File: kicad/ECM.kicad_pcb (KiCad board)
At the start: 2 copper layers, 84.1 x 61.7 mm, 82 parts, among them J1 Bus_PCI_Express_x1, J6 USB_C_Receptacle_USB2.0_16P, Q1 AO3400A, Q2 AO3400A, U1 MCP25625T-E/ML, U10 MAX31855KASA+T, U2 RP2040, U3 ADS8688IDBTR, U4 W25Q128JVP, U5 TPS22976DPUR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

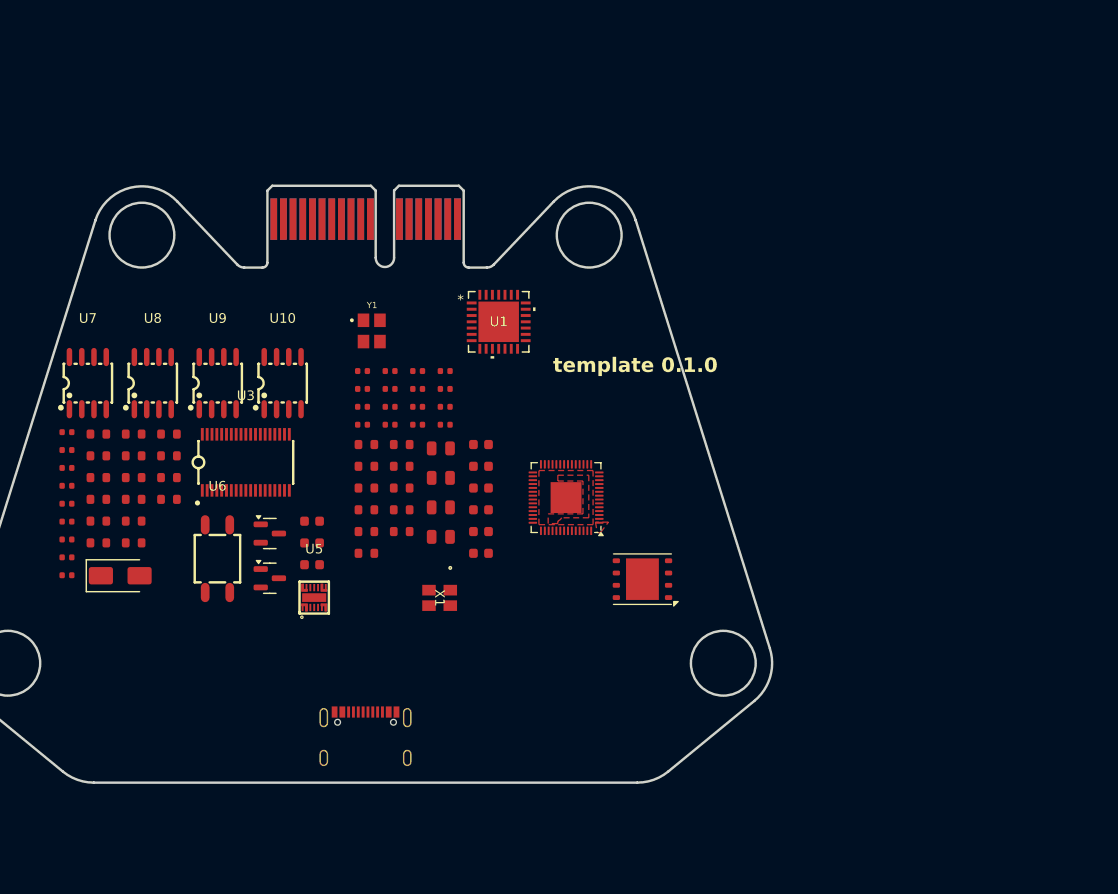
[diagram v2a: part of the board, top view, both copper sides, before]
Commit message: Preliminary PCB Layout on most ICs, carved out analog, power and digital regions.
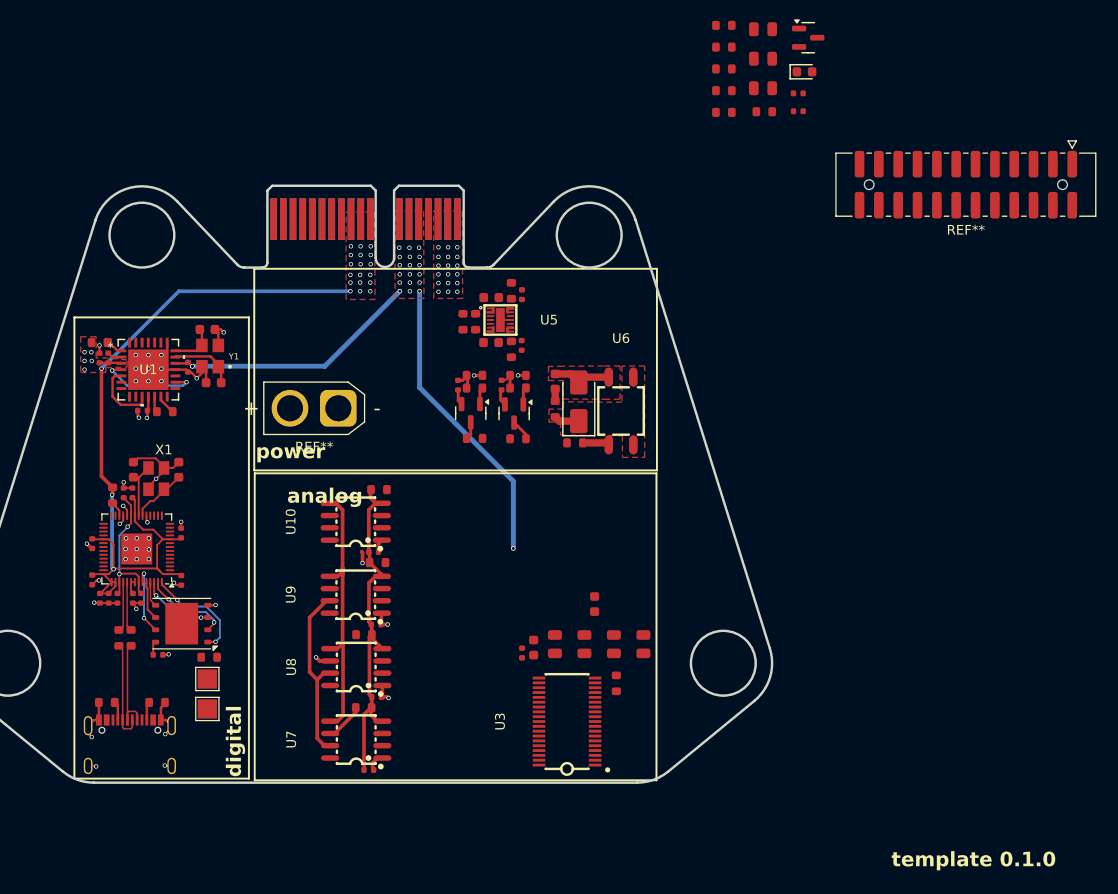
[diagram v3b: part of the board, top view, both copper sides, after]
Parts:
- removed the R7 at (150.2, 87.5)
- removed the R8 at (150.2, 89.7)
- added C36: 2.2uF, PCM_JLCPCB:C_0805, F.Cu at (187.5, 44.5)
- added C37: 100nF, PCM_JLCPCB:C_0402, F.Cu at (191.2, 51.1)
- added C38: 10uF, PCM_JLCPCB:C_0805, F.Cu at (187.5, 47.5)
- added C39: 10uF, PCM_JLCPCB:C_0805, F.Cu at (187.5, 50.6)
- added D2: White, PCM_JLCPCB:D_0603, F.Cu at (191.8, 48.9)
- added Q3: AO3400A, PCM_JLCPCB:Q_SOT-23, F.Cu at (192.2, 45.4)
- added R29: 10kΩ, PCM_JLCPCB:R_0402, F.Cu at (191.2, 53.0)
- added R30: 160kΩ, PCM_JLCPCB:R_0603, F.Cu at (183.5, 44.1)
- added R31: 22kΩ, PCM_JLCPCB:R_0603, F.Cu at (183.5, 46.4)
- added R32: 5.1kΩ, PCM_JLCPCB:R_0603, F.Cu at (183.5, 48.6)
- added R33: 120Ω, PCM_JLCPCB:R_0603, F.Cu at (183.5, 50.9)
- added R34: 5.1kΩ, PCM_JLCPCB:R_0603, F.Cu at (183.5, 53.1)
- added R35: 120Ω, PCM_JLCPCB:R_0603, F.Cu at (187.7, 53.0)
- added REF**: TestPoint_Pad_2.0x2.0mm, TestPoint:TestPoint_Pad_2.0x2.0mm, F.Cu at (130.1, 114.8)
- added REF**: Molex_8783224xx_2x12_P2.0mm_Header_Vertical_Polarized_Mount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, Connector_Molex_Milligrid:Molex_8783224xx_2x12_P2.0mm_Header_Vertical_Polarized_MountingPegs, F.Cu at (208.5, 60.6)
- added REF**: TestPoint_Pad_2.0x2.0mm, TestPoint:TestPoint_Pad_2.0x2.0mm, F.Cu at (130.1, 111.7)
- added REF**: AMASS_XT30U-M_1x02_P5.0mm_Vertical, Connector_AMASS:AMASS_XT30U-M_1x02_P5.0mm_Vertical, F.Cu at (143.6, 83.7)
- moved D1 50.7 mm to (168.5, 83.0), turned to 90 degrees
- moved R7 49.3 mm to (168.1, 87.3)
- moved C29 49.2 mm to (162.6, 71.9), turned to 90 degrees
- moved R14 48.9 mm to (161.5, 71.5), turned to 90 degrees
- moved C30 48.3 mm to (162.6, 77.2), turned to -90 degrees
- moved U4 47.9 mm to (127.4, 106.0)
- moved R22 47.7 mm to (160.5, 81.3), turned to 90 degrees
- moved R8 47.5 mm to (166.0, 83.8), turned to -90 degrees
- moved R15 46.3 mm to (162.2, 81.6)
- moved U7 46.1 mm to (145.4, 118.0), turned to 90 degrees
- moved U2 44.7 mm to (122.8, 98.2)
- moved U6 44.4 mm to (172.8, 84.0)
- moved R23 44.2 mm to (156.0, 81.3), turned to 90 degrees
- moved C32 44.2 mm to (146.8, 121.1), turned to 180 degrees
- moved R21 43.9 mm to (161.5, 77.6), turned to -90 degrees
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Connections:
- net /CS3 renamed /SPI1_CS1
- net /CS4 renamed /SPI1_CS2
- net /CS5 renamed /SPI1_CS3
- net /CS6 renamed /SPI1_CS4
- C24 pad 1: GND -> +5V
- C32 pad 2: Net-(U7-VCC) -> +3.3V
- C33 pad 2: Net-(U8-VCC) -> +3.3V
- C34 pad 2: Net-(U9-VCC) -> +3.3V
- C35 pad 2: Net-(U10-VCC) -> +3.3V
- R10 pad 2: /CS2 -> /SPI1_CS0
- R11 pad 2: /CS1 -> /SPI0_CS0
- U1 pad 1: /CS1 -> /SPI0_CS0
- U1 pad 26: /SCK1 -> /SPI0_SCK
- U1 pad 27: /SDO1 -> /SPI0_MOSI
- U1 pad 28: /SDI1 -> /SPI0_MISO
- U10 pad 4: Net-(U10-VCC) -> +3.3V
- U10 pad 5: /SCK2 -> /SPI1_SCK
- U10 pad 7: /SDO2 -> /SPI1_MISO
- U2 pad 11: unconnected-(U2-GPIO8-Pad11) -> /SPI1_MOSI
- U2 pad 12: unconnected-(U2-GPIO9-Pad12) -> /SPI1_CS0
- U2 pad 13: unconnected-(U2-GPIO10-Pad13) -> /SPI1_SCK
- U2 pad 14: unconnected-(U2-GPIO11-Pad14) -> /SPI1_MISO
- U2 pad 15: unconnected-(U2-GPIO12-Pad15) -> /SPI1_MOSI
- U2 pad 16: unconnected-(U2-GPIO13-Pad16) -> /SPI1_CS0
- U2 pad 17: unconnected-(U2-GPIO14-Pad17) -> /SPI1_SCK
- U2 pad 18: unconnected-(U2-GPIO15-Pad18) -> /SPI1_MISO
- U2 pad 2: unconnected-(U2-GPIO0-Pad2) -> /SPI0_MOSI
- U2 pad 27: unconnected-(U2-GPIO16-Pad27) -> /SPI0_MOSI
- U2 pad 28: unconnected-(U2-GPIO17-Pad28) -> /SPI0_CS0
- U2 pad 29: unconnected-(U2-GPIO18-Pad29) -> /SPI0_SCK
- U2 pad 3: unconnected-(U2-GPIO1-Pad3) -> /SPI0_CS0
- U2 pad 30: unconnected-(U2-GPIO19-Pad30) -> /SPI0_MISO
- U2 pad 31: unconnected-(U2-GPIO20-Pad31) -> /SPI0_MOSI
- U2 pad 32: unconnected-(U2-GPIO21-Pad32) -> /SPI0_CS0
- U2 pad 34: unconnected-(U2-GPIO22-Pad34) -> /SPI0_SCK
- U2 pad 35: unconnected-(U2-GPIO23-Pad35) -> /SPI0_MISO
- U2 pad 36: unconnected-(U2-GPIO24-Pad36) -> /SPI1_MOSI
- U2 pad 37: unconnected-(U2-GPIO25-Pad37) -> /SPI1_CS0
- U2 pad 4: unconnected-(U2-GPIO2-Pad4) -> /SPI0_SCK
- U2 pad 5: unconnected-(U2-GPIO3-Pad5) -> /SPI0_MISO
- U2 pad 6: unconnected-(U2-GPIO4-Pad6) -> /SPI0_MOSI
- U2 pad 7: unconnected-(U2-GPIO5-Pad7) -> /SPI0_CS0
- U2 pad 8: unconnected-(U2-GPIO6-Pad8) -> /SPI0_SCK
- U2 pad 9: unconnected-(U2-GPIO7-Pad9) -> /SPI0_MISO
- U3 pad 1: /SDI2 -> /SPI1_MOSI
- U3 pad 30: GND -> +5V
- U3 pad 36: /SDO2 -> /SPI1_MISO
- U3 pad 37: /SCLK2 -> /SPI1_SCK
- U3 pad 38: /CS2 -> /SPI1_CS0
- U7 pad 4: Net-(U7-VCC) -> +3.3V
- U7 pad 5: /SCK2 -> /SPI1_SCK
- U7 pad 7: /SDO2 -> /SPI1_MISO
- U8 pad 4: Net-(U8-VCC) -> +3.3V
- U8 pad 5: /SCK2 -> /SPI1_SCK
- U8 pad 7: /SDO2 -> /SPI1_MISO
- U9 pad 4: Net-(U9-VCC) -> +3.3V
- U9 pad 5: /SCK2 -> /SPI1_SCK
- U9 pad 7: /SDO2 -> /SPI1_MISO
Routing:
- net +3.3V: track 0.00 -> 133.6 mm, vias 0 -> 28
- net GND: track 0.00 -> 59.3 mm, vias 0 -> 41
- net +5V: track 0.00 -> 57.3 mm, vias 0 -> 21
- net /SPI1_SCK: track 0.00 -> 28.8 mm
- net /SPI1_MISO: track 0.00 -> 18.9 mm
- net +1V1: track 0.00 -> 14.7 mm, vias 0 -> 2
- net /QSPI_SS: track 0.00 -> 11.0 mm, vias 0 -> 2
- net /TXCAN: track 0.00 -> 10.6 mm, vias 0 -> 2
- net /USB_DM: track 0.00 -> 10.5 mm
- net /USB_DP: track 0.00 -> 10.4 mm
- net /QSPI_SD1: track 0.00 -> 9.09 mm, vias 0 -> 2
- net /QSPI_SD2: track 0.00 -> 7.78 mm, vias 0 -> 2
- net /QSPI_SD3: track 0.00 -> 7.26 mm, vias 0 -> 2
- net /RXCAN: track 0.00 -> 7.04 mm
- net /CAN_OSC2: track 0.00 -> 6.83 mm
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- added copper zone on F.Cu, net +24V
- added copper zone on F.Cu, net +5V
- added copper zone on F.Cu, net +BAT
- added copper zone on F.Cu, net GND
- added copper zone on In1.Cu, net GND
- added copper zone on In2.Cu, net GND
- removed copper zone on F.Cu, net +1V1
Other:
- copper layers 2 -> 4
- board text added: "analog"
- board text added: "digital"
- board text added: "power"

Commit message: More progress on layout
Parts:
- moved REF** 69.7 mm to (156.7, 107.2), turned to -90 degrees
- moved R9 18.3 mm to (137.8, 70.4), turned to 180 degrees
- moved R11 14.4 mm to (131.8, 83.2), turned to 180 degrees
- moved C17 13.3 mm to (131.8, 81.6), turned to 90 degrees
- moved C19 13.0 mm to (120.7, 84.6), turned to 180 degrees
- moved C37 12.2 mm to (192.4, 39.0)
- moved C39 12.2 mm to (188.8, 38.5)
- moved D2 12.2 mm to (193.1, 36.8)
- moved R32 12.2 mm to (184.8, 36.5)
- moved R33 12.2 mm to (184.8, 38.8)
- moved R34 12.2 mm to (184.8, 41.0)
- moved R35 12.2 mm to (188.9, 40.9)
- moved C38 12.2 mm to (188.8, 35.5)
- moved R29 12.2 mm to (192.4, 40.9)
- moved R24 11.6 mm to (130.9, 81.6), turned to 90 degrees
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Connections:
- net /SPI1_CS1 renamed /SPI0_CS1
- net /SPI1_CS2 renamed /SPI0_CS2
- net /SPI1_CS3 renamed /SPI0_CS3
- net /SPI1_CS4 renamed /SPI0_CS34
- J1 pad A1: CANP -> /CANH
- J1 pad A3: CANN -> /CANL
- J6 pad A6: /USB_DP -> /USB_DN
- J6 pad B6: /USB_DP -> /USB_DN
- R10 pad 2: /SPI1_CS0 -> /SPI0_CS0
- R11 pad 2: /SPI0_CS0 -> /SPI1_CS0
- R3 pad 2: /USB_DM -> /USB_DN
- U1 pad 1: /SPI0_CS0 -> /SPI1_CS0
- U1 pad 26: /SPI0_SCK -> /SPI1_SCK
- U1 pad 27: /SPI0_MOSI -> /SPI1_MOSI
- U1 pad 28: /SPI0_MISO -> /SPI1_MISO
- U10 pad 5: /SPI1_SCK -> /SPI0_SCK
- U10 pad 7: /SPI1_MISO -> /SPI0_MISO
- U3 pad 1: /SPI1_MOSI -> /SPI0_MOSI
- U3 pad 36: /SPI1_MISO -> /SPI0_MISO
- U3 pad 37: /SPI1_SCK -> /SPI0_SCK
- U3 pad 38: /SPI1_CS0 -> /SPI0_CS0
- U7 pad 5: /SPI1_SCK -> /SPI0_SCK
- U7 pad 7: /SPI1_MISO -> /SPI0_MISO
- U8 pad 5: /SPI1_SCK -> /SPI0_SCK
- U8 pad 7: /SPI1_MISO -> /SPI0_MISO
- U9 pad 5: /SPI1_SCK -> /SPI0_SCK
- U9 pad 7: /SPI1_MISO -> /SPI0_MISO
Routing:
- net /SPI0_MISO: track 0.00 -> 29.2 mm
- net /SPI0_SCK: track 0.00 -> 28.8 mm
- net +3.3V: track 133.6 -> 108.2 mm
- net /CANL: track 1.65 -> 22.9 mm
- net /CANH: track 2.07 -> 22.2 mm
- net /SPI1_CS0: track 0.00 -> 17.6 mm, vias 0 -> 2
- net /SPI1_MOSI: track 0.00 -> 15.2 mm
- net /SPI1_SCK: track 28.8 -> 13.6 mm
- net /USB_DP: track 10.4 -> 0.00 mm
- net +5V: track 57.3 -> 65.8 mm
- net /USB_DM: track 10.5 -> 2.67 mm
- net Net-(U2-USB_DP): track 5.18 -> 0.00 mm
- net Net-(U2-USB_DM): track 5.16 -> 0.00 mm
- net /SPI1_MISO: track 18.9 -> 14.3 mm, vias 0 -> 2
- net GND: track 59.3 -> 55.2 mm, vias 41 -> 58
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
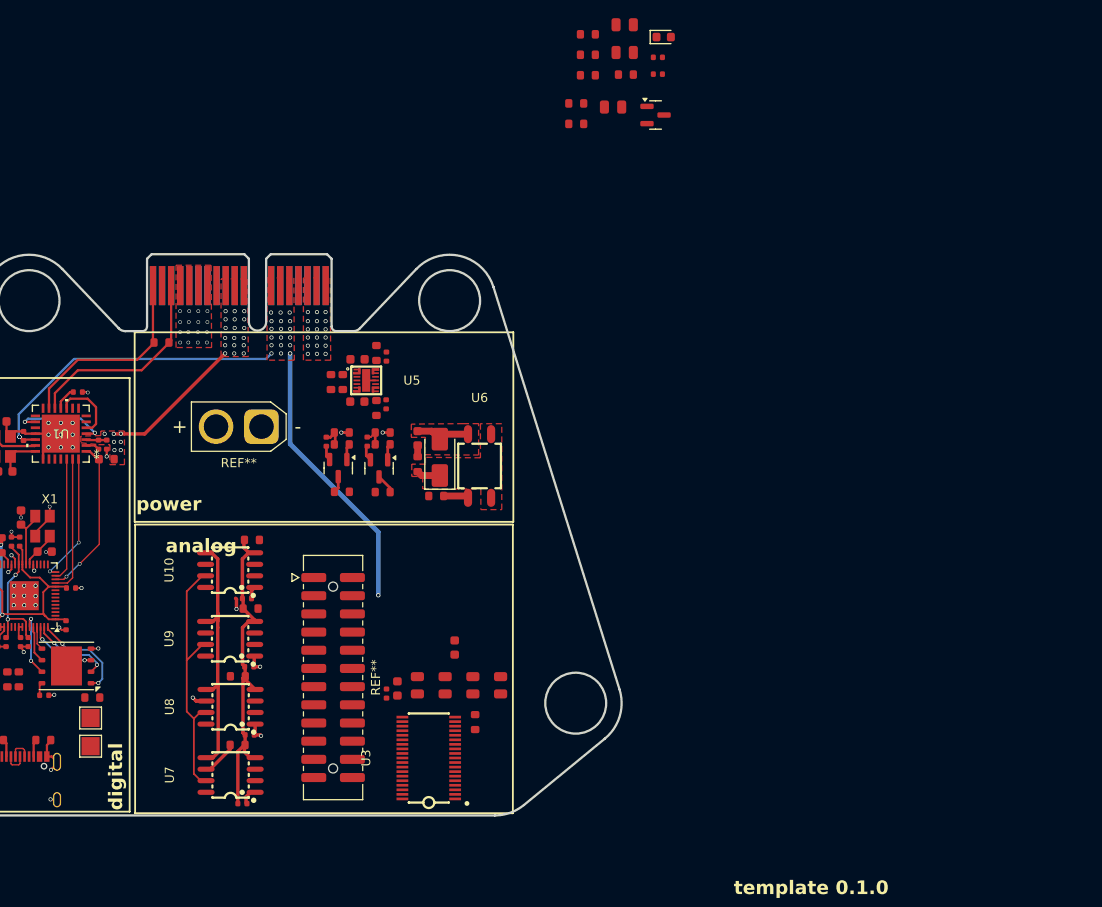
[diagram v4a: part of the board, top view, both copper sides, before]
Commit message: feat: added latching connectors
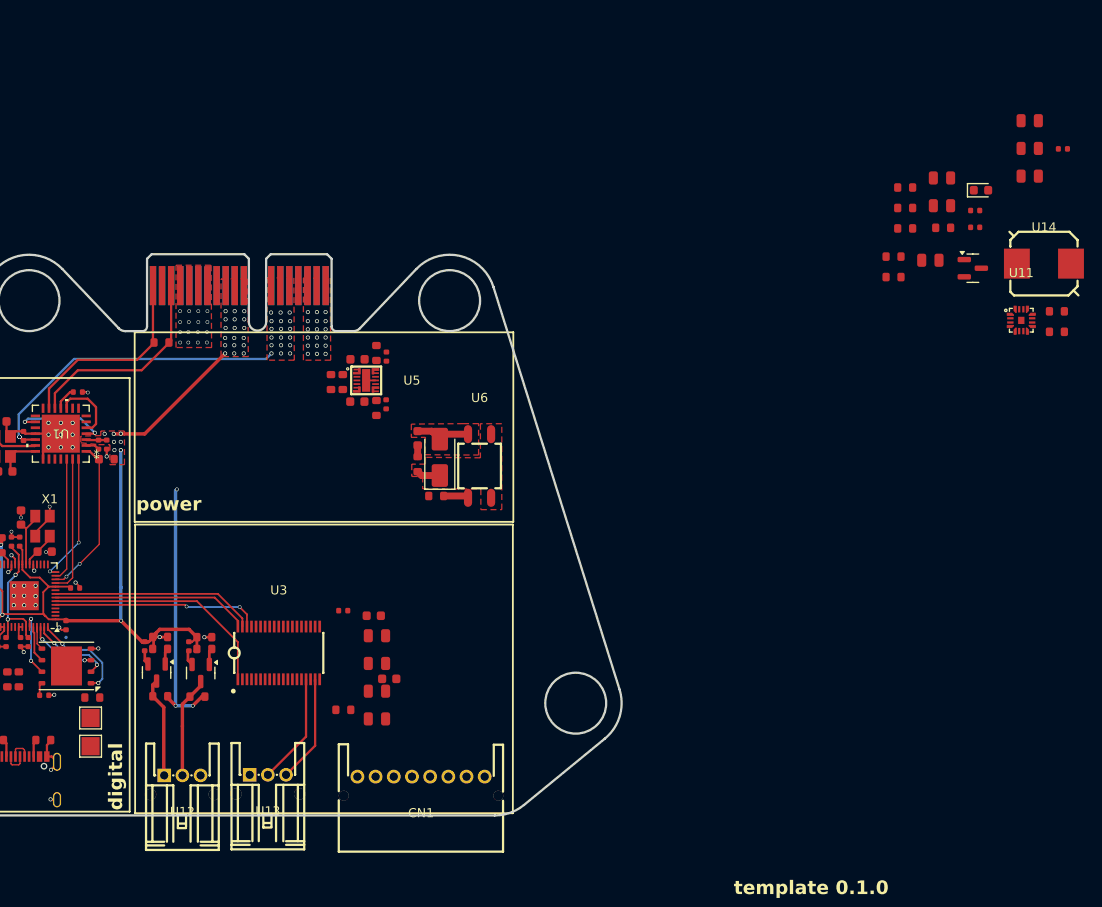
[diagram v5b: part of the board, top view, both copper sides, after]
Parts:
- removed C32, C33, C34, C35: 100nF, PCM_JLCPCB:C_0402
- removed R25, R26, R27, R28: 5.1kΩ, PCM_JLCPCB:R_0603
- removed the REF** at (156.7, 107.2)
- removed the REF** at (148.8, 79.7)
- removed U10, U7, U8, U9: MAX31855KASA+T, easyeda2kicad:SO-8_L4.9-W3.9-P1.27-LS5.9-BL
- added C40: 10uF, PCM_JLCPCB:C_0805, F.Cu at (233.3, 46.0)
- added C41: 10uF, PCM_JLCPCB:C_0805, F.Cu at (233.3, 49.0)
- added C42: 10uF, PCM_JLCPCB:C_0805, F.Cu at (233.3, 52.1)
- added C43: 220pF, PCM_JLCPCB:C_0402, F.Cu at (237.0, 49.1)
- added CN1: S08B-PASK-2(LF)(SN), easyeda2kicad:CONN-TH_S08B-PASK-2, F.Cu at (166.4, 118.2)
- added R36: 160kΩ, PCM_JLCPCB:R_0603, F.Cu at (236.3, 67.0)
- added R37: 1kΩ, PCM_JLCPCB:R_0603, F.Cu at (236.3, 69.2)
- added U11: SY8388ARHC, easyeda2kicad:QFN-16_L2.5-W2.5-P0.45-TL-EP0.6, F.Cu at (232.4, 68.0)
- added U12: S03B-PASK-2, easyeda2kicad:CONN-TH_S03B-PASK-2-LF-SN, F.Cu at (140.2, 118.0)
- added U13: S03B-PASK-2, easyeda2kicad:CONN-TH_S03B-PASK-2-LF-SN, F.Cu at (149.6, 118.0)
- added U14: SPM7054VT-4R7M-D, easyeda2kicad:IND-SMD_L7.5-W7.0_SPM7054VT-330M-D, F.Cu at (234.9, 61.7)
- moved C37 38.8 mm to (227.3, 55.9)
- moved D2 38.8 mm to (228.0, 53.6)
- moved Q3 38.8 mm to (227.1, 62.2)
- moved R29 38.8 mm to (227.3, 57.7)
- moved R30 38.8 mm to (218.4, 61.0)
- moved R31 38.8 mm to (218.4, 63.2)
- moved R32 38.8 mm to (219.7, 53.4)
- moved R33 38.8 mm to (219.7, 55.6)
- moved R34 38.8 mm to (219.7, 57.9)
- moved R35 38.8 mm to (223.8, 57.8)
- moved C36 38.8 mm to (222.4, 61.4)
- moved C39 38.8 mm to (223.7, 55.4)
- moved C38 38.8 mm to (223.7, 52.3)
- moved R20 30.4 mm to (141.8, 109.3), turned to 0 degrees
- moved R17 30.1 mm to (137.7, 102.8)
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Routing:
- net +5V: track 65.8 -> 35.1 mm, vias 21 -> 20
- net +5V_Servo: track 0.00 -> 28.9 mm, vias 0 -> 3
- net /SPI0_MOSI: track 0.00 -> 26.0 mm
- net /SPI0_CS0: track 0.00 -> 21.8 mm
- net /AIN_0IN: track 0.00 -> 12.2 mm
- net /AIN_1IN: track 0.00 -> 12.0 mm
- net /5V_PWM2: track 1.84 -> 11.1 mm
- net /5V_PWM1: track 2.18 -> 11.2 mm
- net GND: track 55.2 -> 48.2 mm, vias 58 -> 56
- net /SPI0_MISO: track 29.2 -> 22.8 mm, vias 0 -> 2
- net /SPI0_SCK: track 28.8 -> 22.6 mm
- net /SPI0_CS2: track 4.03 -> 0.00 mm
- net +3.3V: track 108.2 -> 104.8 mm
- net /SPI0_CS3: track 1.60 -> 0.00 mm, vias 1 -> 0
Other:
- board text removed: "analog"
